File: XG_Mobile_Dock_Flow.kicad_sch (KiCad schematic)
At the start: 72 parts, among them J1 5-1775443-8, J13 39301240, J14 455860005, J17 8730, J2 20455-040E-76, J3 20455-040E-76, J4 3-2362375-4, J5 USB_C_Receptacle, SW1 SW_Push, U1 DS160PR410RNQR, U2 DS160PR410RNQR

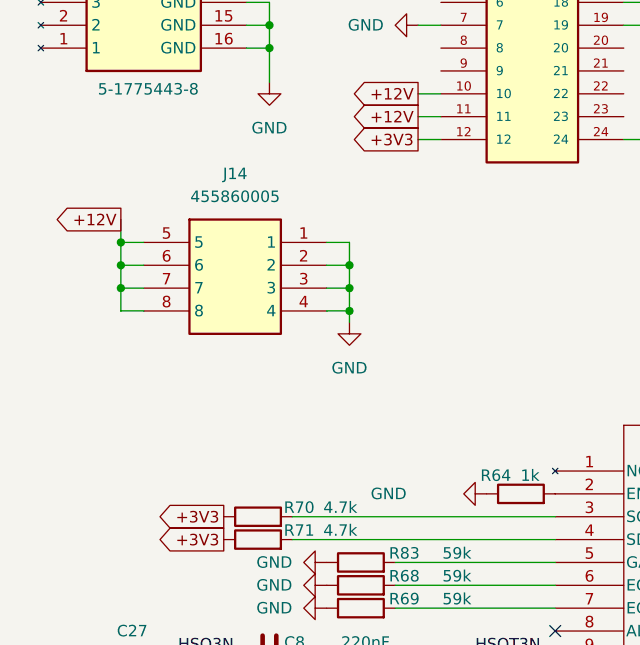
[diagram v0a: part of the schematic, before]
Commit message: updated flow version with proper design
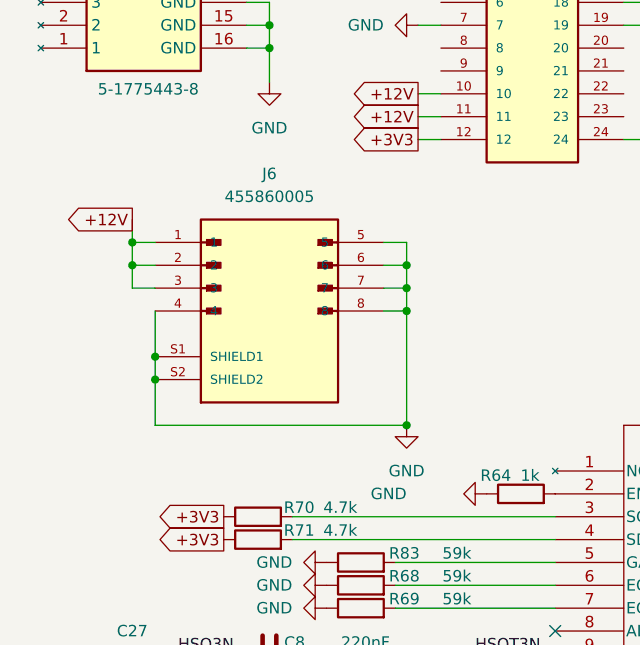
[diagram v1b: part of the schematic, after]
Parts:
- removed J14: 455860005, 469911008:CON_469911008, symbol 3-1775099-2:3-1775099-2
- added J6: 455860005, 455860005:MOLEX_455860005, symbol 455860005:455860005
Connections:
- net +12V: now also J6.1, J6.2, J6.3
- net GND: now also J6.4, J6.5, J6.6, J6.7, J6.8, J6.S1 (SHIELD1), J6.S2 (SHIELD2)

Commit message: added part numbers to pcie power connector
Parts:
- J6: LCSC (none) -> C17693884; Part_Number (none) -> 455860005
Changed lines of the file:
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@@
+			)
+		)
+		(property "Part_Number" "455860005"
+			(at 40.64 182.88 0)
+			(effects
+				(font
+					(size 1.27 1.27)
+				)
+				(hide yes)
+			)
+		)
+		(property "LCSC" "C17693884"
+			(at 40.64 182.88 0)
+			(effects
+				(font
+					(size 1.27 1.27)
+				)
+				(hide yes)
 			)
 		)

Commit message: updated schematics and pcb
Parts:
- U1, U2: LCSC (none) -> C1855779; Part_Number (none) -> DS160PR410RNQR
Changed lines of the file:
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@@
+			)
+		)
+		(property "Part_Number" "DS160PR410RNQR"
+			(at 227.33 195.58 0)
+			(effects
+				(font
+					(size 1.27 1.27)
+				)
+				(hide yes)
+			)
+		)
+		(property "LCSC" "C1855779"
+			(at 227.33 195.58 0)
+			(effects
+				(font
+					(size 1.27 1.27)
+				)
+				(hide yes)
 			)
 		)
@@
 			(at 72.39 200.66 0)
 			(effects
+				(font
+					(size 1.27 1.27)
+				)
+				(hide yes)
+			)
+		)
+		(property "Part_Number" "DS160PR410RNQR"
+			(at 72.39 200.66 0)
+			(effects
+				(font
+					(size 1.27 1.27)
+				)
+				(hide yes)
+			)
+		)
+		(property "LCSC" "C1855779"
+			(at 72.39 200.66 0)
+			(effects

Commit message: more changes
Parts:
- C19: Part_Number GRM188R71C104KA01D -> GRM033R61C104KE84D
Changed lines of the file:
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@@
 			)
 		)
-		(property "Part_Number" "GRM188R71C104KA01D"
+		(property "Part_Number" "GRM033R61C104KE84D"
 			(at 259.08 262.89 0)
 			(effects
